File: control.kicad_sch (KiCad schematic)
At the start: 33 parts, among them J5 MCU disable, J6 TC2030, J7 USB-C, J8 I/O, U4 RPMH3.3-0.5, U5 ESP32-C3-MINI-1U, U6 ECMF02-2AMX6

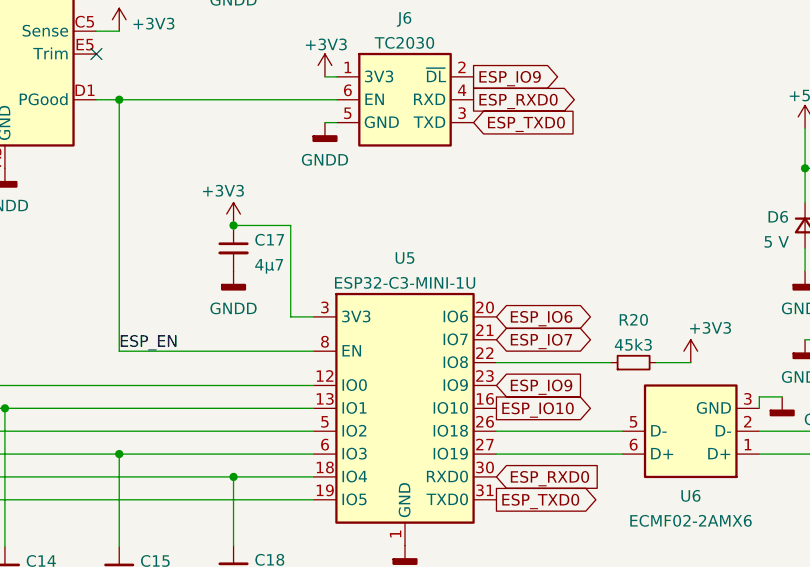
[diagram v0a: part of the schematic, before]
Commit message: Complete footprint assignments
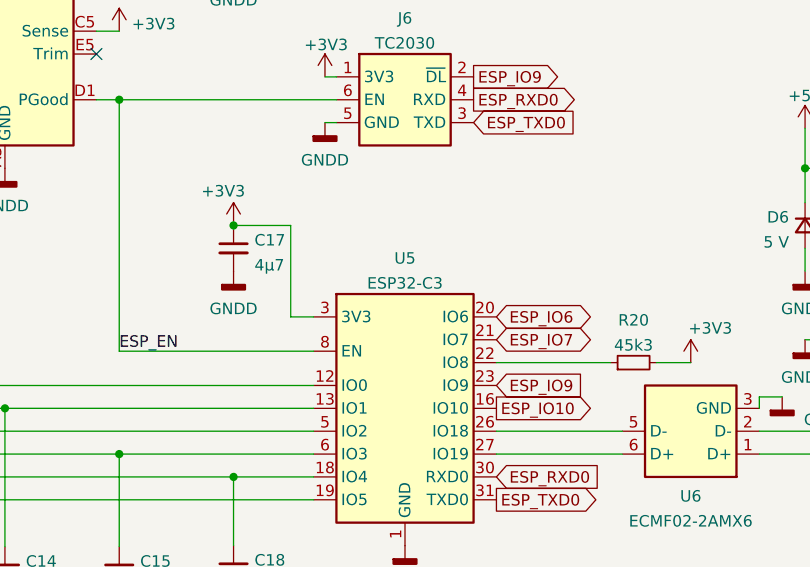
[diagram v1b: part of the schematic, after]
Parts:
- L2: footprint (none) -> phq_SMD:WE-LQS_4018
- U5: value ESP32-C3-MINI-1U -> ESP32-C3; footprint (none) -> phq_Module:ESP32-C3-MINI-1U
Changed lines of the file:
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@@
     (in_bom yes) (on_board yes) (fields_autoplaced)
     (property "Reference" "U5" (id 0) (at 171.45 98.9035 0))
-    (property "Value" "ESP32-C3-MINI-1U" (id 1) (at 171.45 101.6786 0))
-    (property "Footprint" "" (id 2) (at 165.1 113.03 0)
-      (effects (font (size 1.27 1.27)) hide)
-    )
-    (property "Datasheet" "" (id 3) (at 165.1 113.03 0)
+    (property "Value" "ESP32-C3" (id 1) (at 171.45 101.6786 0))
+    (property "Footprint" "phq_Module:ESP32-C3-MINI-1U" (id 2) (at 165.1 113.03 0)
+      (effects (font (size 1.27 1.27)) hide)
+    )
+    (property "Datasheet" "https://www.espressif.com/sites/default/files/documentation/esp32-c3-mini-1_datasheet_en.pdf" (id 3) (at 165.1 113.03 0)
       (effects (font (size 1.27 1.27)) hide)
     )
@@
     (property "Reference" "L2" (id 0) (at 82.55 45.4365 90))
     (property "Value" "15µ" (id 1) (at 82.55 48.2116 90))
-    (property "Footprint" "" (id 2) (at 82.55 50.8 0)
-      (effects (font (size 1.27 1.27)) hide)
-    )
+    (property "Footprint" "phq_SMD:WE-LQS_4018" (id 2) (at 82.55 50.8 0)
+      (effects (font (size 1.27 1.27)) hide)
+    )

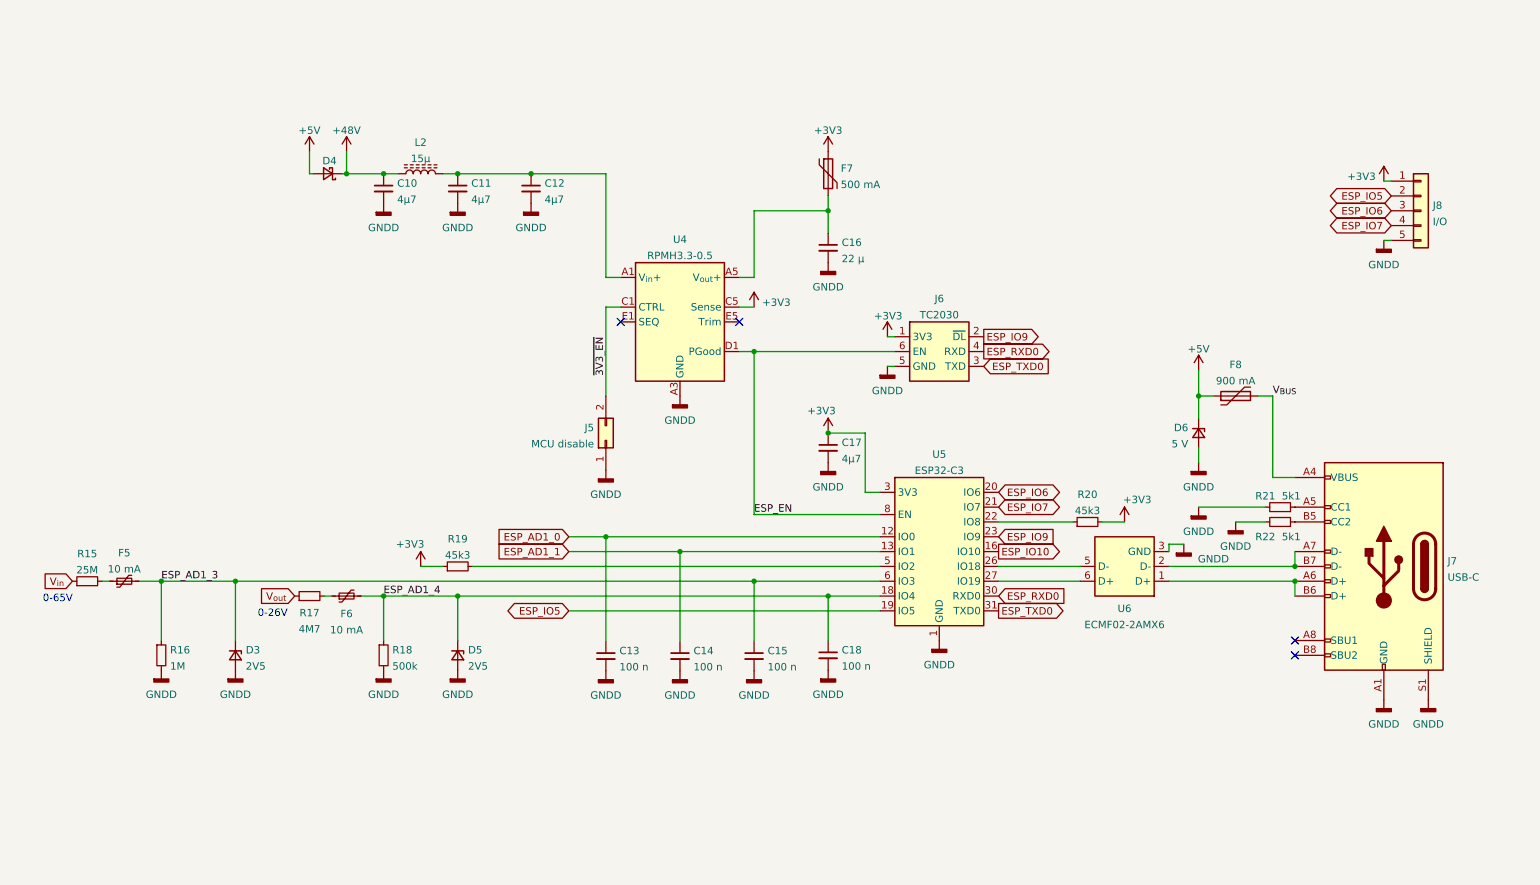
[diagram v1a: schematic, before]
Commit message: Complete placement and routeing
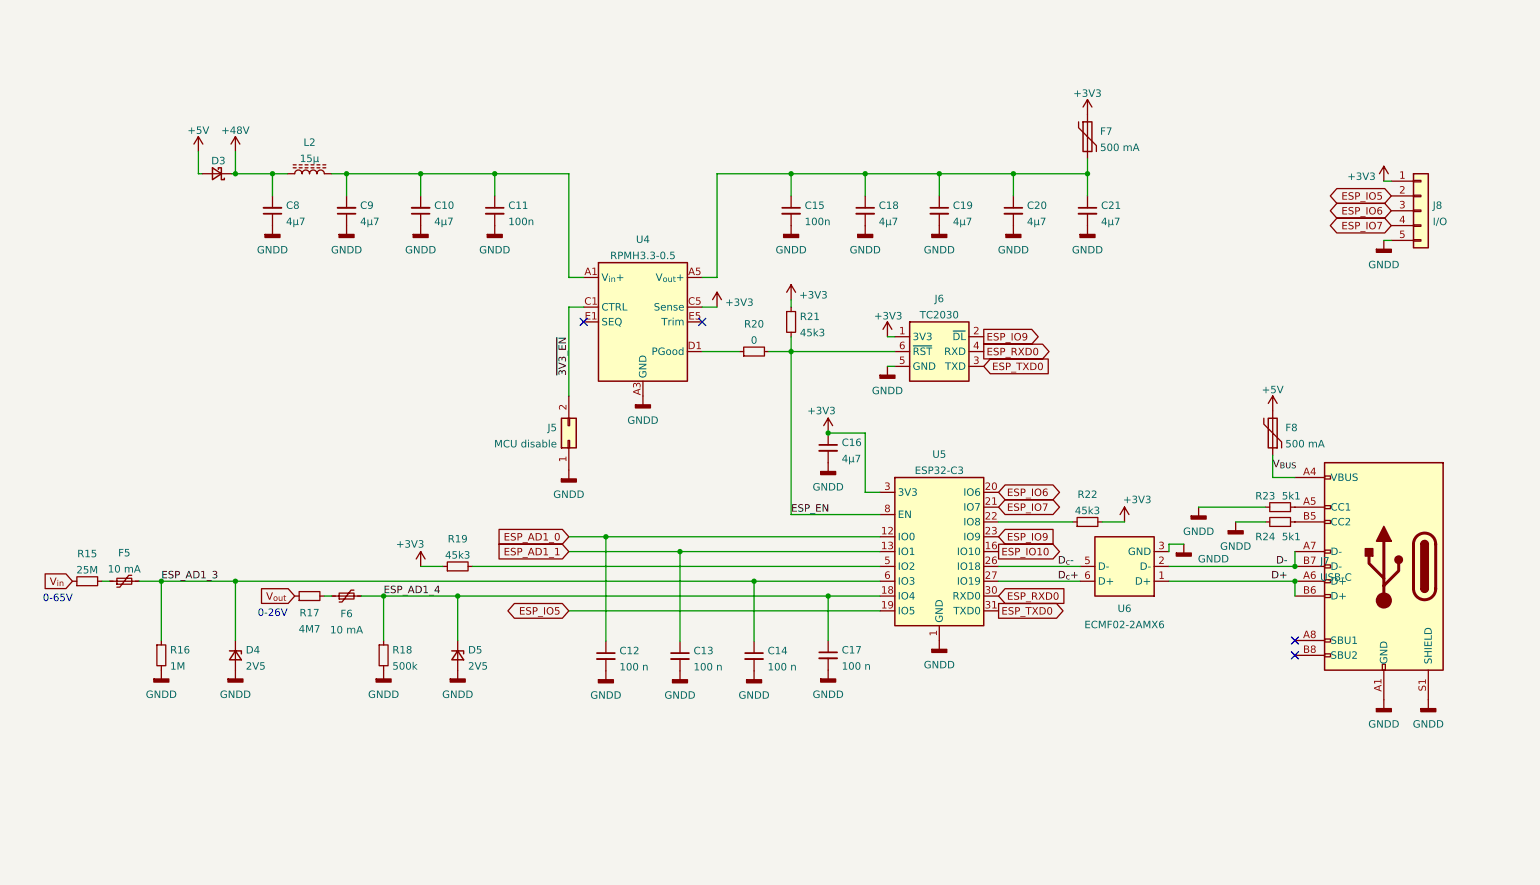
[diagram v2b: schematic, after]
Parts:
- removed C12: 4µ7, Capacitor_SMD:C_1210_3225Metric, symbol Device:C_Small
- removed C16: 22 µ, Capacitor_SMD:C_1206_3216Metric, symbol Device:C_Small
- removed D6: 5 V, Diode_SMD:D_SMA, symbol Device:D_Zener_Small
- added C15: 100n, Capacitor_SMD:C_0402_1005Metric, symbol Device:C_Small
- added C18, C19, C20, C21: 4µ7, Capacitor_SMD:C_0805_2012Metric, symbol Device:C_Small
- added C8, C9: 4µ7, Capacitor_SMD:C_1206_3216Metric, symbol Device:C_Small
- added R20: 0, Resistor_SMD:R_0603_1608Metric, symbol Device:R_Small
- added R21: 45k3, Resistor_SMD:R_0603_1608Metric, symbol Device:R_Small
- C10: footprint Capacitor_SMD:C_1210_3225Metric -> Capacitor_SMD:C_1206_3216Metric; Manufacturer (none) -> Murata; Part Number (none) -> GRJ31CZ72A475KE01L
- C11: value 4µ7 -> 100n; footprint Capacitor_SMD:C_1210_3225Metric -> Capacitor_SMD:C_0402_1005Metric; Manufacturer (none) -> Murata; Part Number (none) -> GRM155R72A102KA01J
- F8: value 900 mA -> 500 mA; footprint Fuse:Fuse_2920_7451Metric -> Fuse:Fuse_0603_1608Metric; Part Number ASMD100F-2 -> MF-FSML050/8-2
- J5: footprint Connector_PinHeader_2.54mm:PinHeader_2x01_P2.54mm_Vertical -> Connector_PinHeader_2.00mm:PinHeader_2x01_P2.00mm_Vertical
- J8: footprint Connector_PinHeader_2.54mm:PinHeader_1x05_P2.54mm_Vertical -> Connector_PinHeader_2.00mm:PinHeader_1x05_P2.00mm_Vertical
- R15, R16, R17, R18, R19: footprint Resistor_SMD:R_0805_2012Metric -> Resistor_SMD:R_0603_1608Metric
- R22: renamed from R20; footprint Resistor_SMD:R_0805_2012Metric -> Resistor_SMD:R_0603_1608Metric
- R23: renamed from R21; footprint Resistor_SMD:R_0805_2012Metric -> Resistor_SMD:R_0603_1608Metric
- R24: renamed from R22; footprint Resistor_SMD:R_0805_2012Metric -> Resistor_SMD:R_0603_1608Metric
- renumbered C13 to C12, C14 to C13, C15 to C14, C17 to C16, C18 to C17, D4 to D3, D3 to D4
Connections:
- net +3V3: now also R21.1
- net +48V: now also C8.2; no longer C10.1
- net +5V: now also F8.2; no longer F8.1
- net ESP_EN: now also R20.2, R21.2; no longer U4.D1 (PGood)
- net GND: now also C10.1, U5.49_1 (GND), U5.49_2 (GND), U5.49_3 (GND), U5.49_4 (GND), U5.49_5 (GND), U5.49_6 (GND), U5.49_7 (GND), U5.49_8 (GND), U5.49_9 (GND), C15.2, C18.2, C19.2, C20.2, C21.2, C8.1, C9.1; no longer C10.2, U5.49 (GND)
- net V_{BUS}: now also F8.1; no longer F8.2
- net at C11.1, L2.2, U4.A1 (V_{in}+)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: now also C10.2, C9.2
- net at F7.2, U4.A5 (V_{out}+), U4.B5 (V_{out}+): now also C15.1, C18.1, C19.1, C20.1, C21.1
- net D+: now reaches J7.A6 (D+), J7.B6 (D+), U6.1 (D+)
- net D-: now reaches J7.A7 (D-), J7.B7 (D-), U6.2 (D-)
- net D_{c}-: now reaches U5.26 (IO18), U6.5 (D-)
- net D_{c}+: now reaches U5.27 (IO19), U6.6 (D+)
- new net: R20.1, U4.D1 (PGood)
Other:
- moved on the sheet: D3, F7, F8, J5, L2, U4

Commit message: Exclude ancillary I/O header from BOM
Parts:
- J8: now left out of the parts list
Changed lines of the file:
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@@
   )
   (symbol (lib_id "Connector_Generic:Conn_01x05") (at 254 57.15 0) (unit 1)
-    (in_bom yes) (on_board yes) (fields_autoplaced)
+    (in_bom no) (on_board yes) (fields_autoplaced)
     (property "Reference" "J8" (id 0) (at 256.032 56.2415 0)
       (effects (font (size 1.27 1.27)) (justify left))

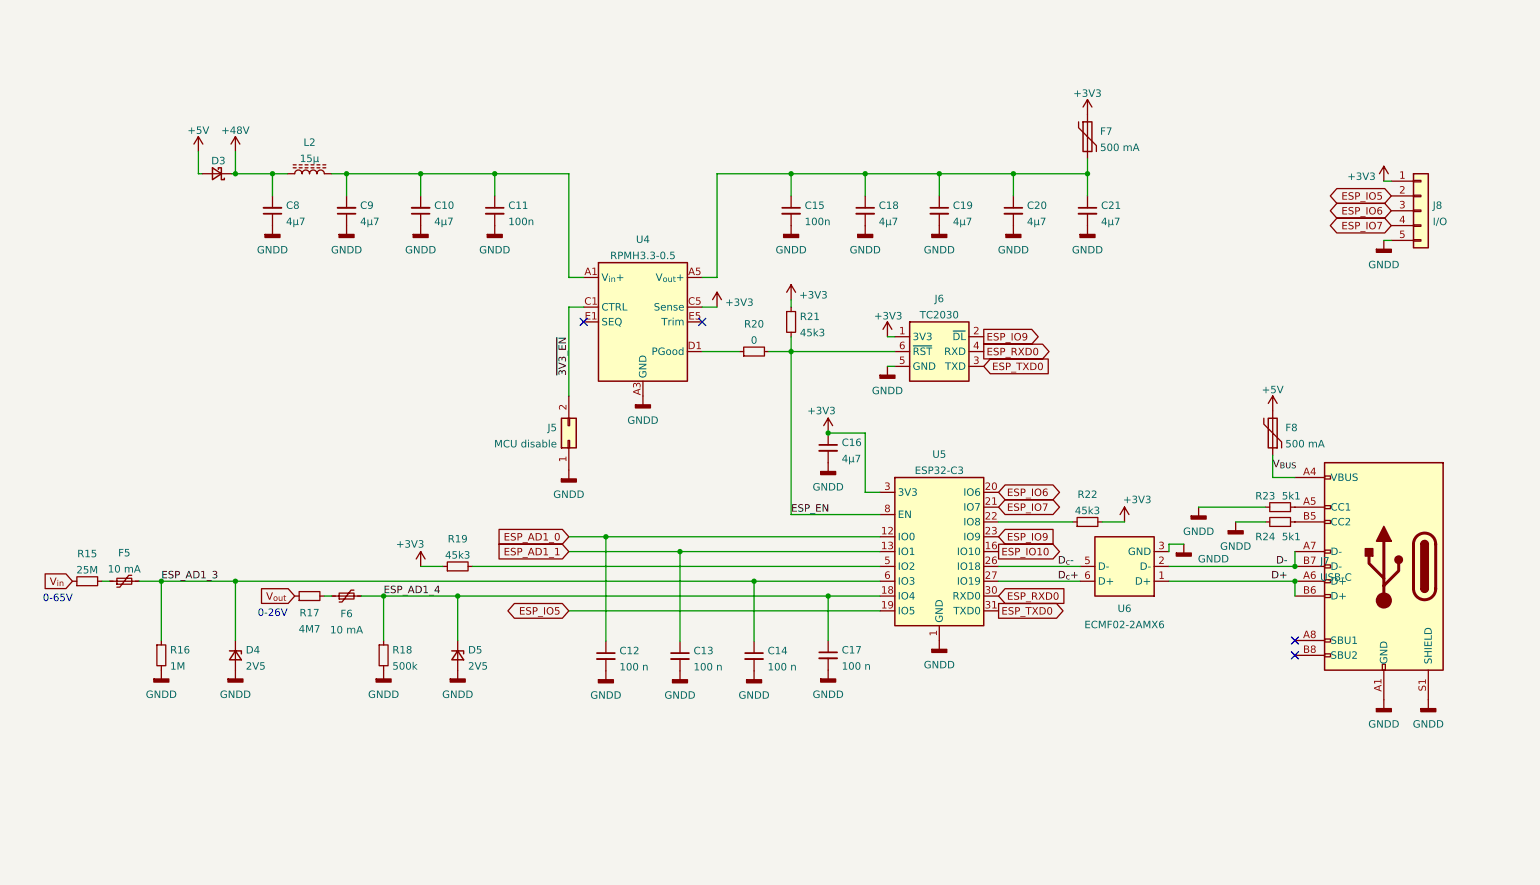
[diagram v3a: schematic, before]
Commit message: Add 3.3 V TVS diodes and revise ground zones
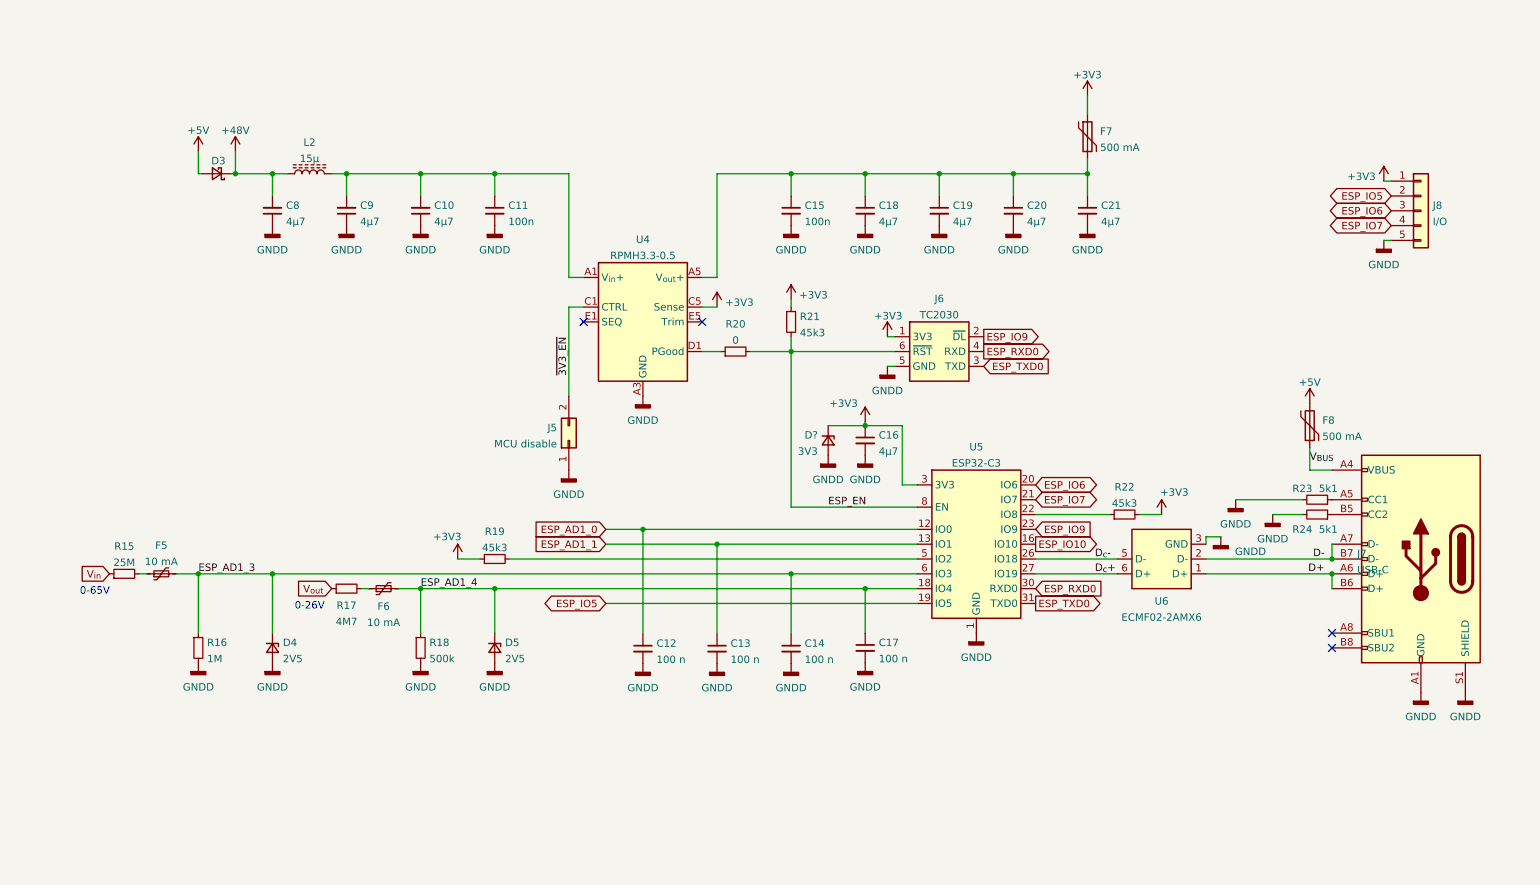
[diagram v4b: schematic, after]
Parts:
- added D?: 3V3, Diode_SMD:D_0402_1005Metric, symbol Device:D_Zener_Small
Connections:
- net +3V3: now also D?.1 (K)
- net GND: now also D?.2 (A)
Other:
- moved on the sheet: C12, C13, C14, C16, C17, D4, D5, F5, F6, F8, J7, R15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

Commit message: Clean up schematic
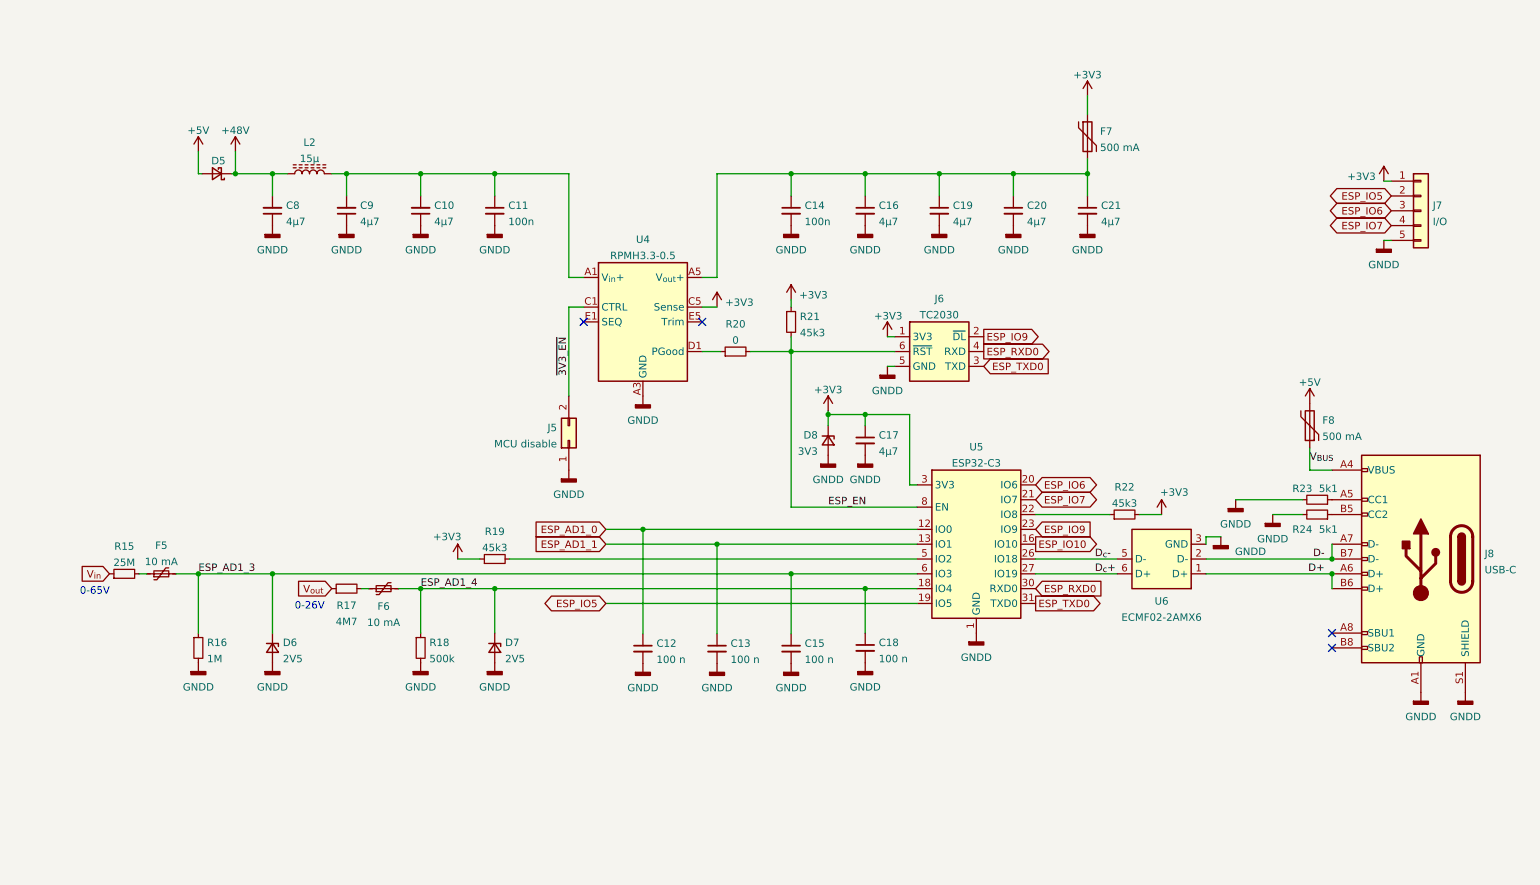
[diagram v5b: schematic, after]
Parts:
- gave numbers to parts that had none: 1
- renumbered C15 to C14, C14 to C15, C18 to C16, C16 to C17, C17 to C18, D3 to D5, D4 to D6, D5 to D7, J8 to J7, J7 to J8
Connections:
- net GND: now also J8.S2 (SHIELD), J8.S3 (SHIELD), J8.S4 (SHIELD)
